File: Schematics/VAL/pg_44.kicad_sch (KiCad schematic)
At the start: 18 parts

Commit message: VAL: polish.  Tested to 8.39 seconds (rm090)
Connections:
- net A.LE: now also U.1 (D0); no longer U.5 (D3)
- net ACS.DIAG_OFF~: now also U.4 (D4); no longer U.5 (D5)
- net ARF_WE.EN~: now also U.1 (D0); no longer U.2 (D1)
- net B.LE: now also U.1 (D0); no longer U.5 (D3)
- net CLK.2XE: now also U.5 (D3), U.5 (D3); no longer U.1 (D0), U.1 (D0)
- net CLK.2XE~: now also U.2 (D3); no longer U.1 (D0)
- net CS_STOP~: now also U.5 (D5); no longer U.1 (D0)
- net H1.PHD: now also U.4 (D2), U.4 (D2); no longer U.2 (D1), U.2 (D1)
- net PU: no longer U.2 (D3), U.2 (D3), U.4 (D2), U.4 (D2)
- net RAM_STOP~: now also U.1 (D0); no longer U.5 (D5)
- net WE.EN~: now also U.2 (D1); no longer U.1 (D0)
- net at U.4 (D4): no longer U.3 (Q)
- net at U.6 (Q): now also U.2 (D3); no longer U.4 (D4)
- net at U.4 (Q): now also U.1 (D0); no longer U.2 (D3)
- new net: U.3 (Q), U.5 (D5)
- no-connect marks 8 -> 12
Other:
- moved on the sheet: U

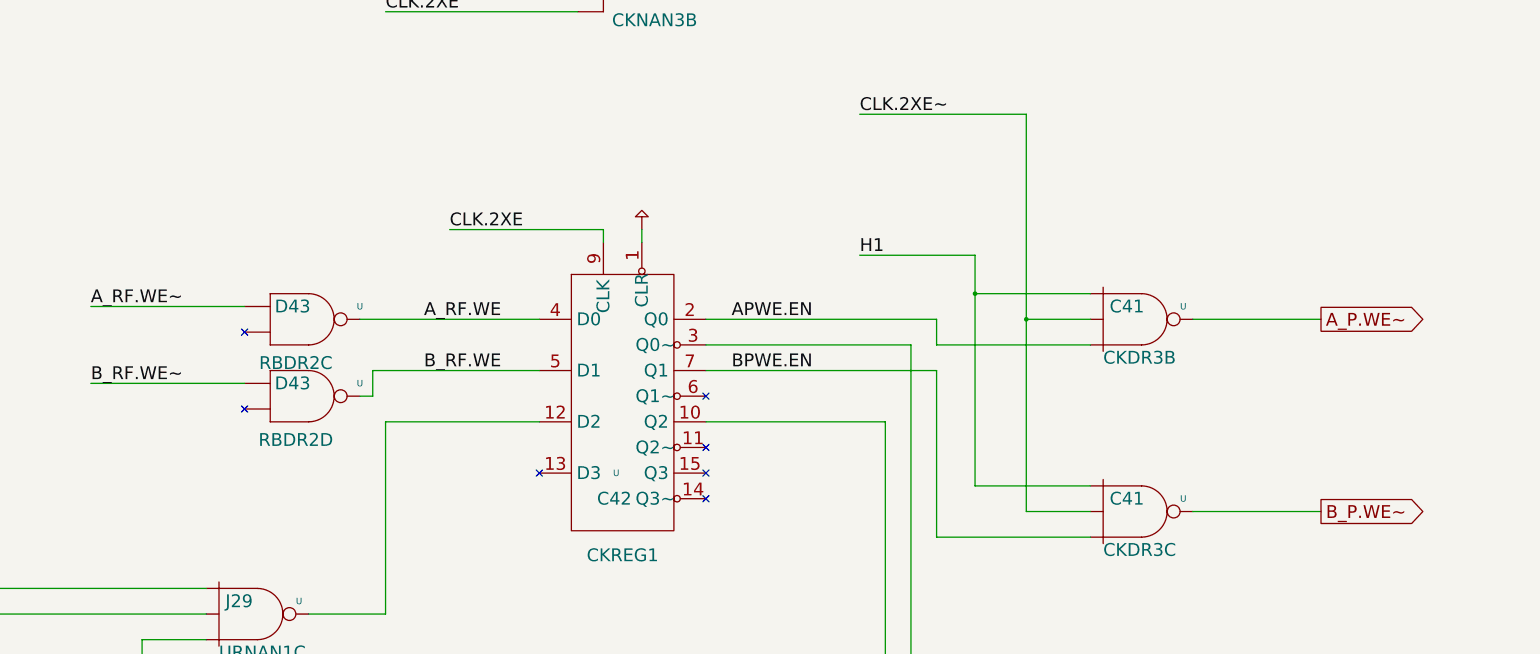
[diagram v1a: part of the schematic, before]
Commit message: VAL : disable pargen, tested to 6.55 (rm101)
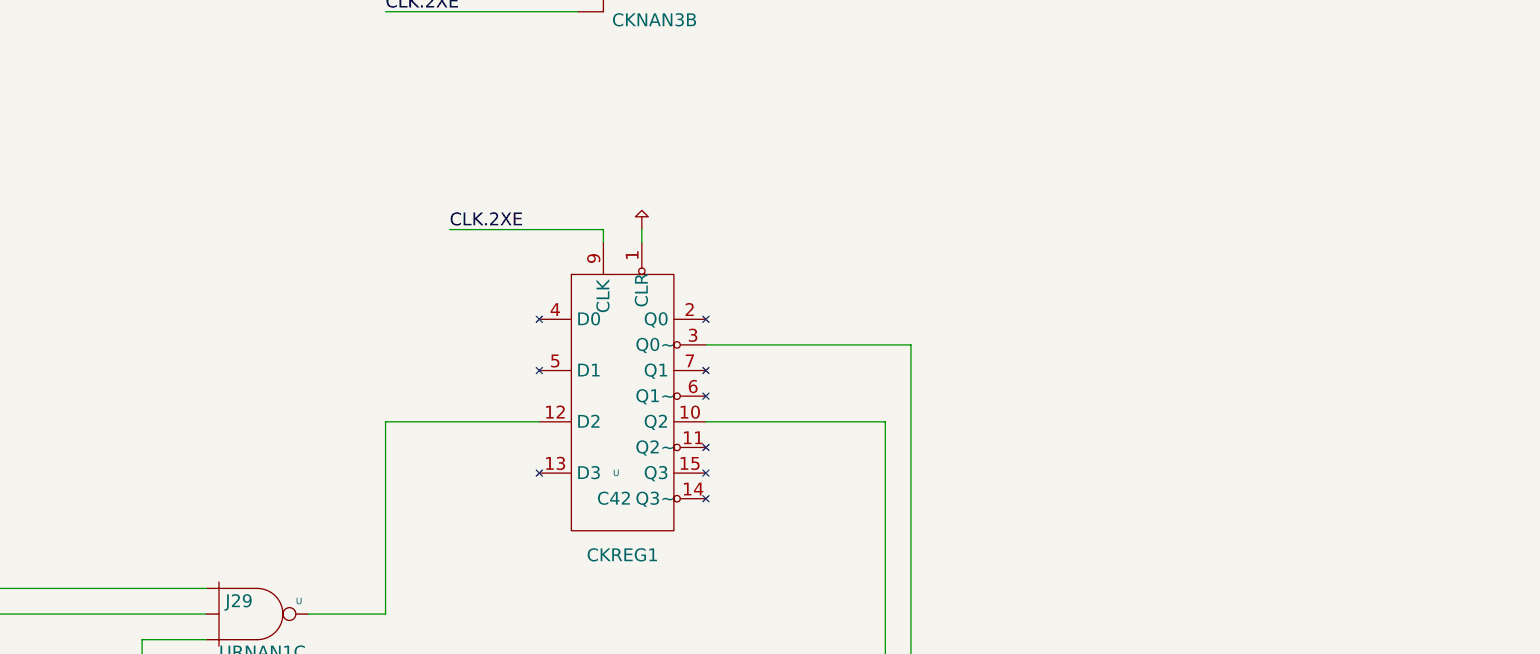
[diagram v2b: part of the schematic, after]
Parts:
- removed U (x2): (no value), symbol r1000:F37
- removed U (x2): (no value), symbol r1000:F10
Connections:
- net APWE.EN: no longer names the net of U.2 (Q0)
- net A_RF.WE: no longer names the net of U.4 (D0)
- net BPWE.EN: no longer names the net of U.7 (Q1)
- net B_RF.WE: no longer names the net of U.5 (D1)
- no-connect marks 12 -> 14

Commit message: VAL: prune DFSM
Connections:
- net ACS.DIAG_OFF~: no longer names the net of U.4 (D4)
- net BCS.DIAG_OFF~: no longer names the net of U.2 (D3)
- no-connect marks 14 -> 16
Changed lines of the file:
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@@
   (no_connect (at 223.52 271.78))
   (no_connect (at 223.52 287.02))
+  (no_connect (at 279.4 154.94))
   (no_connect (at 528.32 132.08))
   (no_connect (at 223.52 281.94))
+  (no_connect (at 279.4 124.46))
   (no_connect (at 223.52 256.54))
   (no_connect (at 223.52 266.7))
@@
     (stroke (width 0) (type default))
   )
-  (wire (pts (xy 274.32 154.94) (xy 279.4 154.94))
-    (stroke (width 0) (type default))
-  )
   (wire (pts (xy 220.98 91.44) (xy 231.14 91.44))
     (stroke (width 0) (type default))
@@
   )
   (wire (pts (xy 193.04 111.76) (xy 198.12 111.76))
-    (stroke (width 0) (type default))
-  )
-  (wire (pts (xy 274.32 124.46) (xy 279.4 124.46))
     (stroke (width 0) (type default))
   )
@@
     )
   )
-  (global_label "BCS.DIAG_OFF~" (shape input) (at 274.32 154.94 180) (fields_autoplaced)
-    (effects (font (size 2.54 2.54)) (justify right))
-    (property "Intersheet References" "${INTERSHEET_REFS}" (id 0) (at 241.554 154.7813 0)
-      (effects (font (size 1.905 1.905)) (justify right))
-    )
-  )
   (global_label "CS_STOP~" (shape input) (at 266.7 139.7 180) (fields_autoplaced)
     (effects (font (size 2.54 2.54)) (justify right))
@@
       (effects (font (size 1.905 1.905)) (justify right))
     )
-  )
-  (global_label "ACS.DIAG_OFF~" (shape input) (at 274.32 124.46 180) (fields_autoplaced)
-    (effects (font (size 2.54 2.54)) (justify right))
-    (property "Intersheet References" "${INTERSHEET_REFS}" (id 0) (at 241.9169 124.3013 0)
-      (effects (font (size 1.905 1.905)) (justify right))
-    )
